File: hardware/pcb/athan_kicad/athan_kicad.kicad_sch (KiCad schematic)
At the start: 26 parts, among them J1 USB_C_Receptacle_PowerOnly_6P, J2 AudioJack4, SW1 ui_select, SW2 ui_next, SW3 SW_SPST

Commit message: PCB schematic updated with fixes of the previous version. The Layout is not done yet. Check the previous commit for a previous version layout
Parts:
- removed OLED1: SSD1306_I2C, Connector_PinHeader_2.54mm:PinHeader_1x04_P2.54mm_Vertical, symbol Connector_Generic:Conn_01x04
- removed OLED_spi3: SSD1306_SPI, Connector_PinHeader_2.54mm:PinHeader_1x07_P2.54mm_Vertical, symbol Connector_Generic:Conn_01x07
- added J_Rx1, J_Tx1: SolderJumper_2_Bridged, Jumper:SolderJumper-2_P1.3mm_Bridged2Bar_RoundedPad1.0x1.5mm, symbol Jumper:SolderJumper_2_Bridged
- OLED1: renamed from OLED2; footprint Display:Adafruit_SSD1306 -> Display:Adafruit_SSD1306_multi
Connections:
- net ESP_Rx: now also J_Rx1.2 (B); no longer DFP1.3 (TX)
- net ESP_Tx: now also J_Tx1.2 (B); no longer DFP1.2 (RX)
- new net: DFP1.3 (TX), J_Rx1.1 (A)
- new net: DFP1.2 (RX), J_Tx1.1 (A)
- no-connect marks 24 -> 23

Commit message: PCB V2 in progress
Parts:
- removed AXU2: Conn_01x03, TerminalBlock:TerminalBlock_MaiXu_MX126-5.0-03P_1x03_P5.00mm, symbol Connector:Screw_Terminal_01x03
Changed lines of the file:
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@@
-	)
-	(junction
-		(at 220.98 81.28)
-		(diameter 0)
-		(color 0 0 0 0)
 	)
 	(junction
@@
 		(pts
 			(xy 68.58 148.59) (xy 68.58 116.84)
-		)
-		(stroke
-			(width 0)
-			(type default)
-		)
-	)
-	(wire
-		(pts
-			(xy 220.98 81.28) (xy 231.14 81.28)
 		)
 		(stroke
@@
 					(unit 1)
 				)
-			)
-		)
-	)
-	(symbol
-		(lib_id "Connector:Screw_Terminal_01x03")
-		(at 236.22 83.82 0)
-		(unit 1)
-		(exclude_from_sim no)
-		(in_bom yes)
-		(on_board yes)
-		(dnp no)
-		(fields_autoplaced yes)
-		(property "Reference" "AXU2"
-			(at 238.76 82.5499 0)
-			(effects
-				(font
-					(size 1.27 1.27)
-				)
-				(justify left)
-			)
-		)
-		(property "Value" "Conn_01x03"
-			(at 238.76 85.0899 0)
-			(effects
-				(font
-					(size 1.27 1.27)
-				)
-				(justify left)
-			)
-		)
-		(property "Footprint" "TerminalBlock:TerminalBlock_MaiXu_MX126-5.0-03P_1x03_P5.00mm"
-			(at 236.22 83.82 0)
-			(effects
-				(font
-					(size 1.27 1.27)
-				)
-				(hide yes)
-			)
-		)
-		(property "Datasheet" "~"
-			(at 236.22 83.82 0)
-			(effects
-				(font
-					(size 1.27 1.27)
-				)
-				(hide yes)
-			)
-		)
-		(property "Description" "Generic screw terminal, single row, 01x03, script generated (kicad-library-utils/schlib/autogen/connector/)"
-			(at 236.22 83.82 0)
-			(effects
-				(font
-					(size 1.27 1.27)
-				)
-				(hide yes)
-			)
-		)
-		(pin "3"
-		)
-		(pin "2"
-		)
-		(pin "1"
-		)
-		(instances
-			(project ""
-				(path "/25639631-c40b-4bb2-a86a-70d5f89de4ae"
-					(reference "AXU2")
-					(unit 1)
-				)

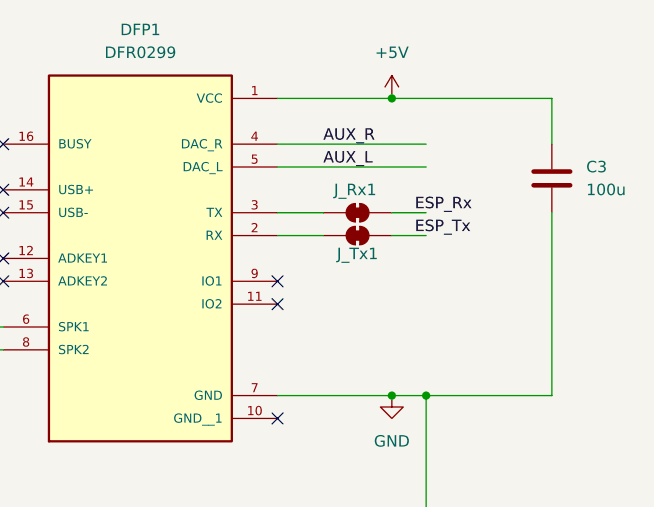
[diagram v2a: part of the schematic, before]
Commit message: enhancing schematic: adding 1k resistor before dfplayer Rx for eleminating potential buzzing. changing AUX jack footprint from PJ320E to PJ320A which is a mirrored image (more available on stores). PCB not complete yet
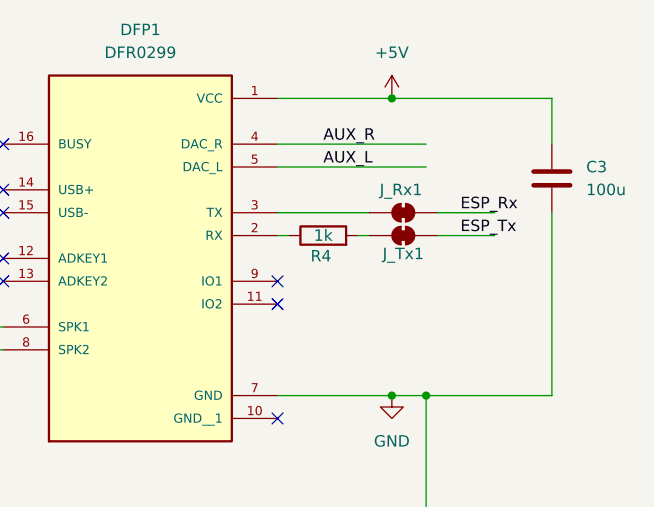
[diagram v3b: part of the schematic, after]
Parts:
- added R4: 1k, Resistor_THT:R_Axial_DIN0207_L6.3mm_D2.5mm_P7.62mm_Horizontal, symbol Device:R
- J2: footprint Connector_Audio:Jack_3.5mm_PJ320E_Horizontal -> Connector_Audio:Jack_3.5mm_PJ320A_Horizontal
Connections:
- net at DFP1.2 (RX): now also R4.1; no longer J_Tx1.1 (A)
- new net: J_Tx1.1 (A), R4.2
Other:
- moved on the sheet: J_Rx1, J_Tx1
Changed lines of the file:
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@@
+	(wire
+		(pts
+			(xy 222.25 43.18) (xy 228.6 43.18)
+		)
+		(stroke
+			(width 0)
+			(type default)
+		)
+	)
 	(wire
 		(pts
@@
 	(wire
 		(pts
+			(xy 213.36 43.18) (xy 214.63 43.18)
+		)
+		(stroke
+			(width 0)
+			(type default)
+		)
+	)
+	(wire
+		(pts
 			(xy 205.74 144.78) (xy 213.36 144.78)
 		)
@@
 	(wire
 		(pts
-			(xy 217.17 40.64) (xy 220.98 40.64)
+			(xy 222.25 40.64) (xy 228.6 40.64)
 		)
 		(stroke
@@
 	(wire
 		(pts
-			(xy 204.47 43.18) (xy 209.55 43.18)
-		)
-		(stroke
-			(width 0)
-			(type default)
-		)
-	)
-	(wire
-		(pts
 			(xy 120.65 179.07) (xy 120.65 156.21)
 		)
@@
 	(wire
 		(pts
-			(xy 204.47 40.64) (xy 209.55 40.64)
+			(xy 204.47 40.64) (xy 214.63 40.64)
 		)
 		(stroke
@@
 	(wire
 		(pts
-			(xy 217.17 43.18) (xy 220.98 43.18)
-		)
-		(stroke
-			(width 0)
-			(type default)
-		)
-	)
-	(wire
-		(pts
 			(xy 217.17 60.96) (xy 220.98 60.96)
 		)
@@
 		(pts
 			(xy 91.44 153.67) (xy 95.25 153.67)
+		)
+		(stroke
+			(width 0)
+			(type default)
+		)
+	)
+	(wire
+		(pts
+			(xy 204.47 43.18) (xy 205.74 43.18)
 		)
 		(stroke
@@
 	)
 	(label "ESP_Tx"
-		(at 219.71 43.18 0)
+		(at 224.79 43.18 0)
 		(effects
 			(font
@@
 	)
 	(label "ESP_Rx"
-		(at 219.71 40.64 0)
+		(at 224.79 40.64 0)
 		(effects
 			(font
@@
 	(symbol
 		(lib_id "Jumper:SolderJumper_2_Bridged")
-		(at 213.36 40.64 0)
+		(at 218.44 40.64 0)
 		(unit 1)
 		(exclude_from_sim no)
@@
 		(dnp no)
 		(property "Reference" "J_Rx1"
-			(at 213.106 38.1 0)
+			(at 218.186 38.1 0)
 			(effects
 				(font
@@
 		)
 		(property "Value" "SolderJumper_2_Bridged"
-			(at 213.36 36.83 0)
+			(at 218.44 36.83 0)
 			(effects
 				(font
@@
 		)
 		(property "Footprint" "Jumper:SolderJumper-2_P1.3mm_Bridged2Bar_RoundedPad1.0x1.5mm"
-			(at 213.36 40.64 0)
+			(at 218.44 40.64 0)
 			(effects
 				(font
@@
 		)
 		(property "Datasheet" "~"
-			(at 213.36 40.64 0)
+			(at 218.44 40.64 0)
 			(effects
 				(font
@@
 		)
 		(property "Description" "Solder Jumper, 2-pole, closed/bridged"
-			(at 213.36 40.64 0)
+			(at 218.44 40.64 0)
 			(effects
 				(font
@@
 			)
 		)
-		(property "Footprint" "Connector_Audio:Jack_3.5mm_PJ320E_Horizontal"
+		(property "Footprint" "Connector_Audio:Jack_3.5mm_PJ320A_Horizontal"
 			(at 198.12 83.82 0)
 			(effects
@@
 	)
 	(symbol
+		(lib_id "Device:R")
+		(at 209.55 43.18 90)
+		(unit 1)
+		(exclude_from_sim no)
+		(in_bom yes)
+		(on_board yes)
+		(dnp no)
+		(property "Reference" "R4"
+			(at 209.296 45.466 90)
+			(effects
+				(font
+					(size 1.27 1.27)
+				)
+			)
+		)
+		(property "Value" "1k"
+			(at 209.55 43.18 90)
+			(effects
+				(font
+					(size 1.27 1.27)
+				)
+			)
+		)
+		(property "Footprint" "Resistor_THT:R_Axial_DIN0207_L6.3mm_D2.5mm_P7.62mm_Horizontal"
+			(at 209.55 44.958 90)
+			(effects
+				(font
+					(size 1.27 1.27)
+				)
+				(hide yes)
+			)
+		)
+		(property "Datasheet" "~"
+			(at 209.55 43.18 0)
+			(effects
+				(font
+					(size 1.27 1.27)
+				)
+				(hide yes)
+			)
+		)
+		(property "Description" "200 to 1k is fine"
+			(at 208.28 45.212 90)
+			(effects
+				(font
+					(size 1.27 1.27)
+				)
+				(hide yes)
+			)
+		)
+		(pin "1"
+		)
+		(pin "2"
+		)
+		(instances
+			(project "athan_kicad"
+				(path "/25639631-c40b-4bb2-a86a-70d5f89de4ae"
+					(reference "R4")
+					(unit 1)
+				)
+			)
+		)
+	)
+	(symbol
 		(lib_id "Connector:Screw_Terminal_01x02")
 		(at 121.92 53.34 0)
@@
 	(symbol
 		(lib_id "Jumper:SolderJumper_2_Bridged")
-		(at 213.36 43.18 0)
+		(at 218.44 43.18 0)
 		(unit 1)
 		(exclude_from_sim no)
@@
 		(dnp no)
 		(property "Reference" "J_Tx1"
-			(at 213.36 45.212 0)
+			(at 218.44 45.212 0)
 			(effects
 				(font
@@
 		)
 		(property "Value" "SolderJumper_2_Bridged"
-			(at 213.36 39.37 0)
+			(at 218.44 39.37 0)
 			(effects
 				(font
@@
 		)
 		(property "Footprint" "Jumper:SolderJumper-2_P1.3mm_Bridged2Bar_RoundedPad1.0x1.5mm"
-			(at 213.36 43.18 0)
+			(at 218.44 43.18 0)
 			(effects
 				(font
@@
 		)
 		(property "Datasheet" "~"
-			(at 213.36 43.18 0)
+			(at 218.44 43.18 0)
 			(effects
 				(font
@@
 		)
 		(property "Description" "Solder Jumper, 2-pole, closed/bridged"
-			(at 213.36 43.18 0)
-			(effects
-				(font
+			(at 218.44 43.18 0)
+			(effects
+				(font
